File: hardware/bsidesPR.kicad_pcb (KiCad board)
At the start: 2 copper layers, 136 x 120.2 mm, 76 parts, among them J2 Conn_ARM_SWD_TagConnect_TC2030, J3 Conn_01x03_Female, Q1 2N7002H, Q2 DMP2012SN-7, SW1 SW_MEC_5G, U1 Pico, U2 TPS61040DDC

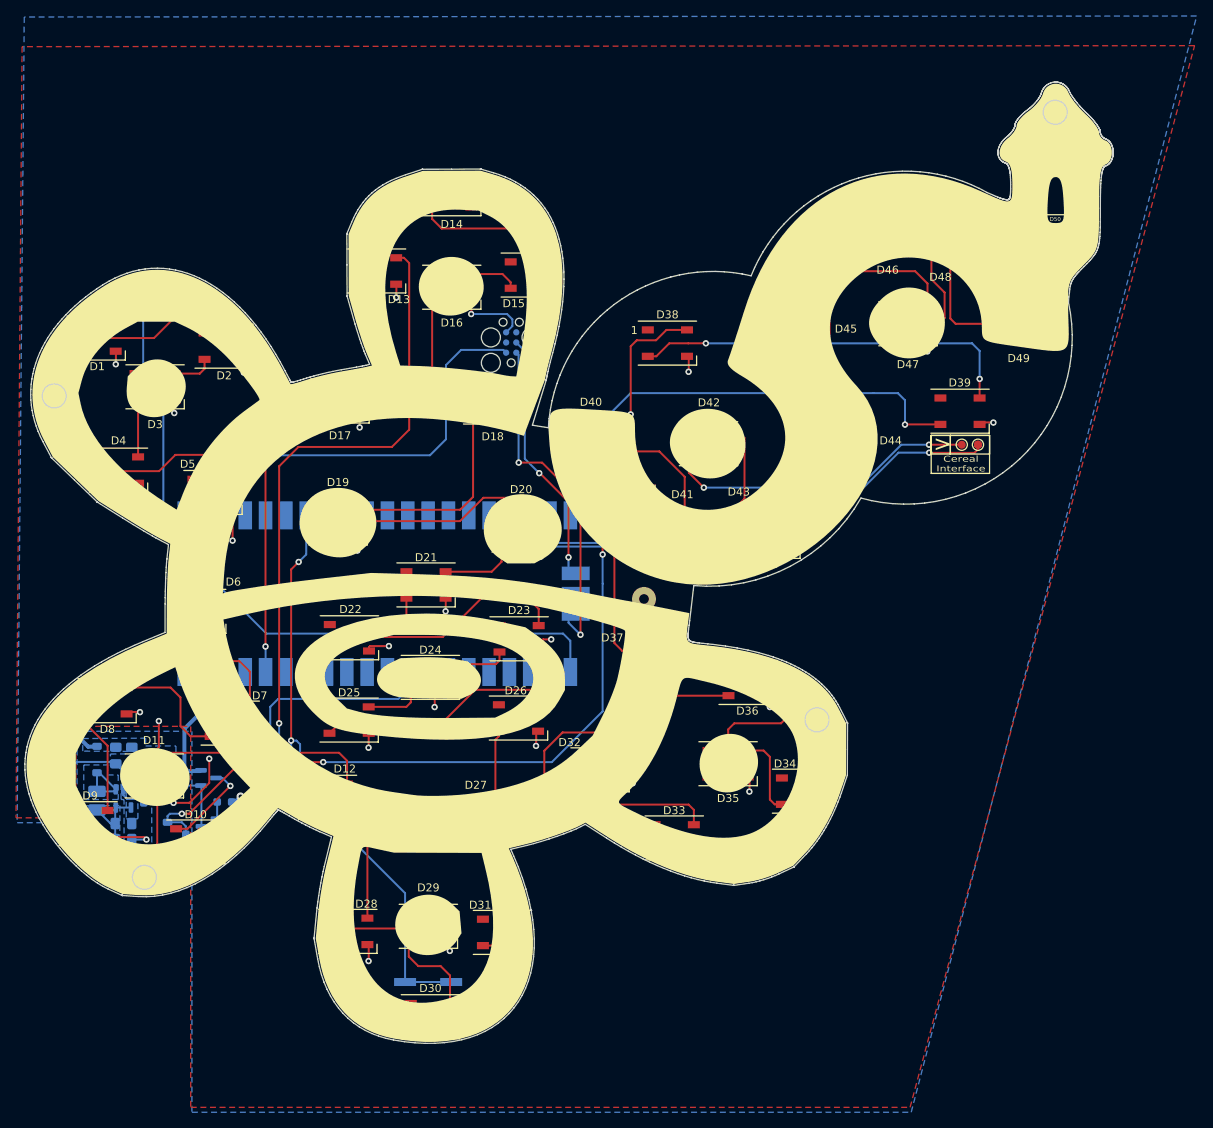
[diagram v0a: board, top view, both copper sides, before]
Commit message: Adding some animation support as well as final hardware files
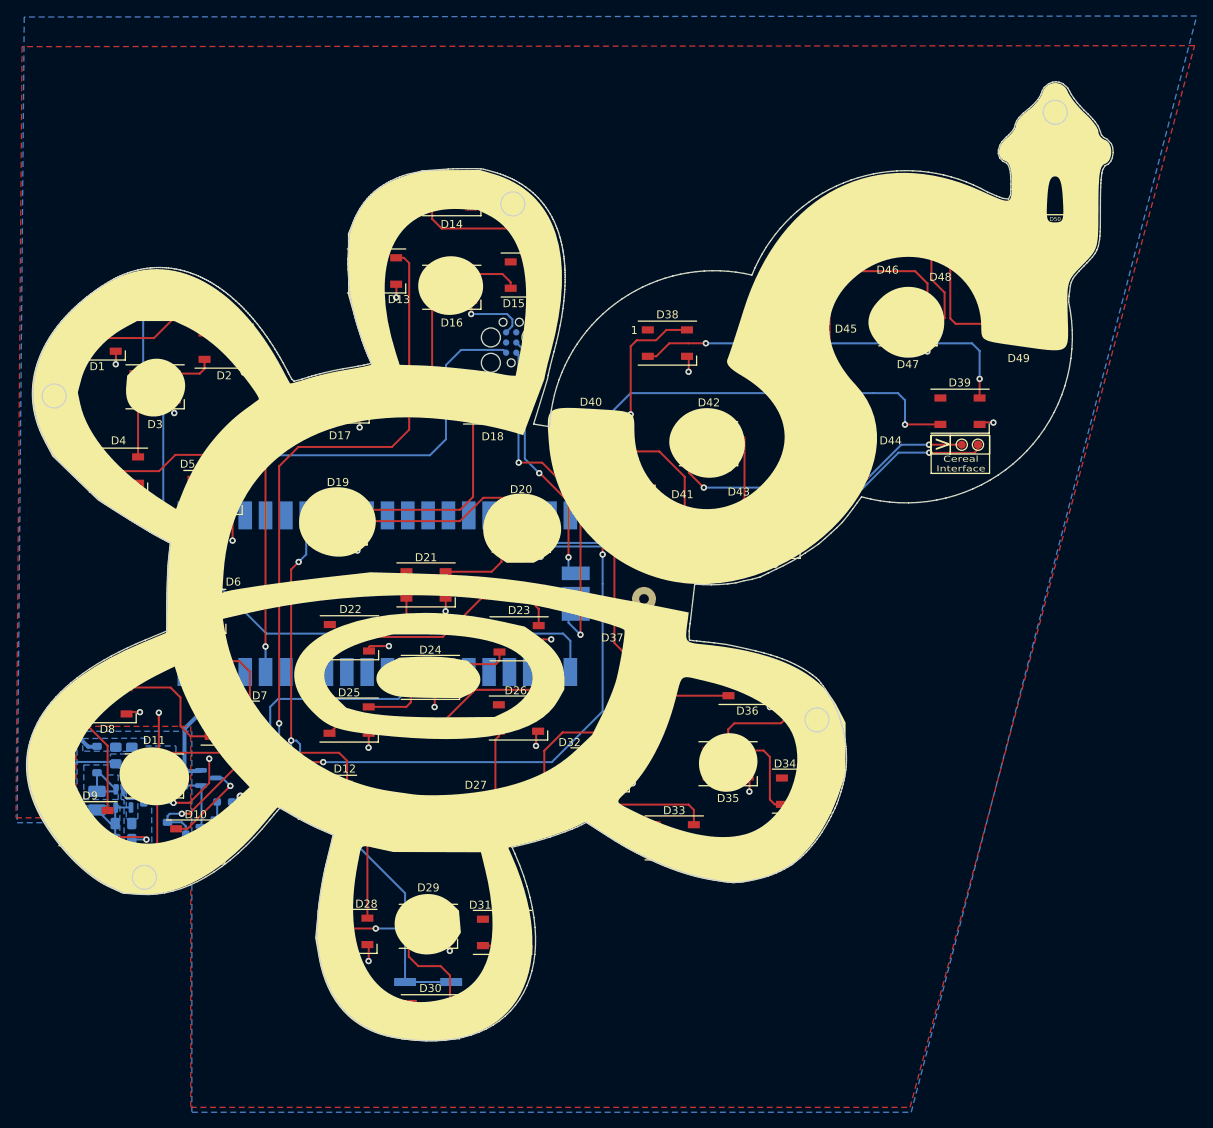
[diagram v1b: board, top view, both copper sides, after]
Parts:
- removed the G*** at (178.9, 67.5)
- added G***: LOGO, LOGO, B.Cu at (164.9, 67.6)
- added G***: LOGO, LOGO, B.Cu at (128.8, 137.9)
- added G***: LOGO, LOGO, B.Cu at (96.3, 72.4)
- added G***: LOGO, LOGO, B.Cu at (194.8, 60.5)
- added G***: LOGO, LOGO, B.Cu at (165.6, 118.6)
- added G***: LOGO, LOGO, B.Cu at (140.7, 57.2)
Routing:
- net VLED: track 18.5 -> 20.4 mm
- net Net-(D28-DOUT): track 16.6 -> 17.2 mm, vias 0 -> 2
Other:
- board size 136 x 120.2 mm -> 135.8 x 119.9 mm
- board text added: "Badge brought to you by: @So11Deo6loria @nathantsmith @Kshockles @yoyo_bond @headinthebooth"
- board text added: "https://github.com/So11Deo6loria/bsidesPRSun"
- board text removed: "<YOUR LOGO HERE>"
- board text removed: "Badge brought to you by: @So11Deo6loria @Nate_Sm1th @kshock @YoYo @headinthebooth"

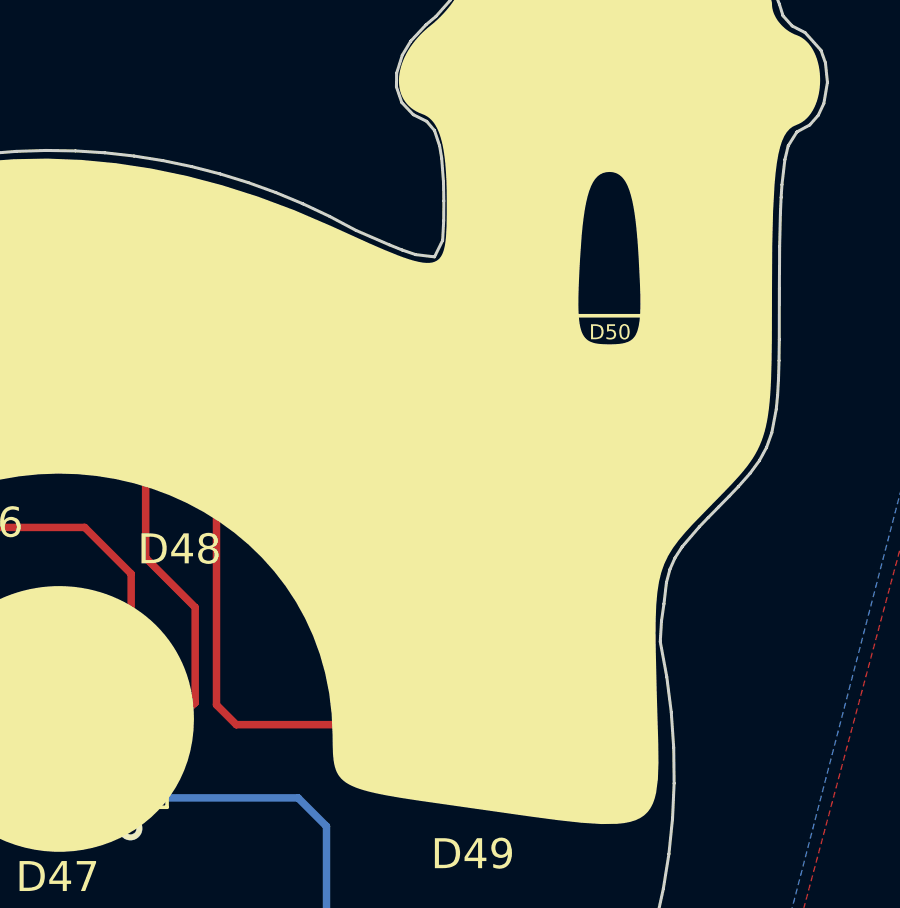
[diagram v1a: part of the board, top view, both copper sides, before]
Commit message: Firmware is close. We just need to add the flags, test one more time, and add back the lowpower stuff that messes with rshell.
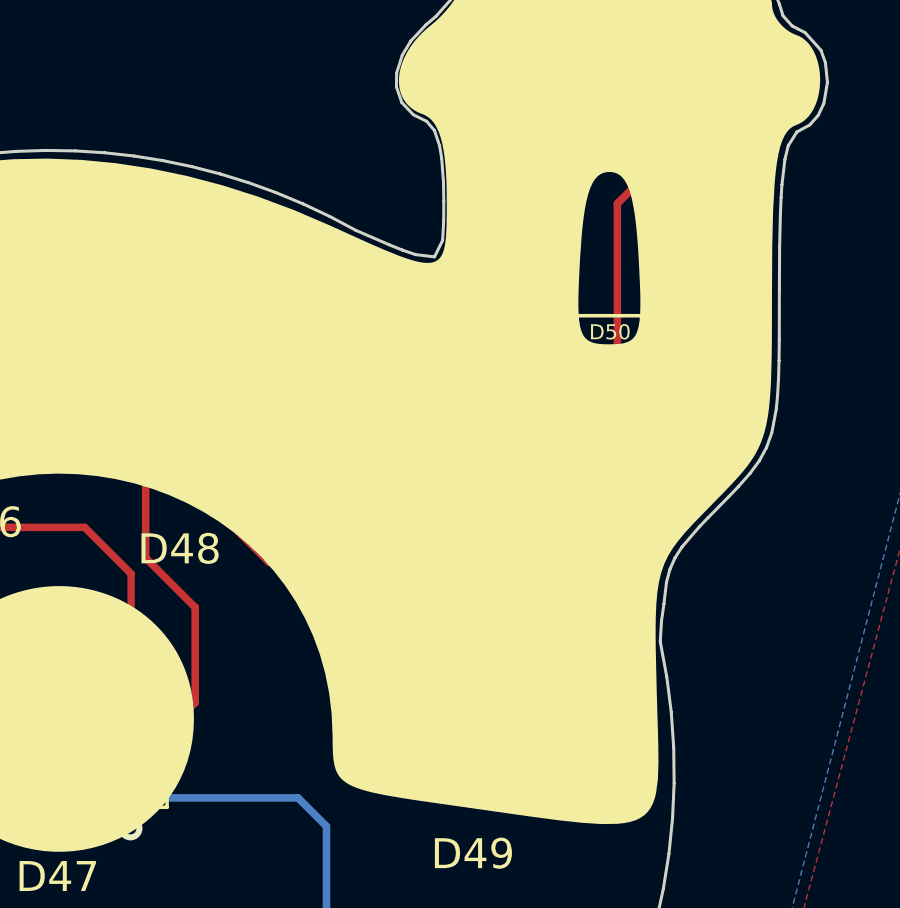
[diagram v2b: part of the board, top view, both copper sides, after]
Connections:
- D49 pad 2: Net-(D48-DOUT) -> Net-(D49-DOUT)
- D49 pad 4: Net-(D49-DIN) -> Net-(D48-DOUT)
- D50 pad 2: Net-(D49-DIN) -> unconnected-(D50-DOUT-Pad2)
- D50 pad 4: unconnected-(D50-DIN-Pad4) -> Net-(D49-DOUT)
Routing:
- net Net-(D49-DOUT): track 0.00 -> 25.6 mm
- net Net-(D49-DIN): track 11.6 -> 0.00 mm
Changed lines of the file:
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@@
   (net 77 "Net-(D25-DOUT)")
   (net 78 "Net-(D26-DOUT)")
-  (net 79 "unconnected-(D50-DIN-Pad4)")
-  (net 80 "Net-(D49-DIN)")
+  (net 79 "Net-(D49-DOUT)")
+  (net 80 "unconnected-(D50-DOUT-Pad2)")
   (net 81 "Net-(D43-DOUT)")
   (net 82 "Net-(D32-DOUT)")
@@
       (net 20 "VLED") (pinfunction "VDD") (pintype "power_in"))
     (pad "2" smd rect (at -2.45 1.65) (size 1.5 0.9) (layers "F.Cu" "F.Paste" "F.Mask")
-      (net 80 "Net-(D49-DIN)") (pinfunction "DOUT") (pintype "output"))
+      (net 80 "unconnected-(D50-DOUT-Pad2)") (pinfunction "DOUT") (pintype "output"))
     (pad "3" smd rect (at 2.45 1.65) (size 1.5 0.9) (layers "F.Cu" "F.Paste" "F.Mask")
       (net 1 "GND") (pinfunction "VSS") (pintype "power_in"))
     (pad "4" smd rect (at 2.45 -1.65) (size 1.5 0.9) (layers "F.Cu" "F.Paste" "F.Mask")
-      (net 79 "unconnected-(D50-DIN-Pad4)") (pinfunction "DIN") (pintype "input"))
+      (net 79 "Net-(D49-DOUT)") (pinfunction "DIN") (pintype "input"))
     (model "${KICAD7_3DMODEL_DIR}/LED_SMD.3dshapes/LED_WS2812B_PLCC4_5.0x5.0mm_P3.2mm.wrl"
       (offset (xyz 0 0 0))
@@
       (net 20 "VLED") (pinfunction "VDD") (pintype "power_in"))
     (pad "2" smd rect (at -2.45 1.65) (size 1.5 0.9) (layers "F.Cu" "F.Paste" "F.Mask")
-      (net 42 "Net-(D48-DOUT)") (pinfunction "DOUT") (pintype "output"))
+      (net 79 "Net-(D49-DOUT)") (pinfunction "DOUT") (pintype "output"))
     (pad "3" smd rect (at 2.45 1.65) (size 1.5 0.9) (layers "F.Cu" "F.Paste" "F.Mask")
       (net 1 "GND") (pinfunction "VSS") (pintype "power_in"))
     (pad "4" smd rect (at 2.45 -1.65) (size 1.5 0.9) (layers "F.Cu" "F.Paste" "F.Mask")
-      (net 80 "Net-(D49-DIN)") (pinfunction "DIN") (pintype "input"))
+      (net 42 "Net-(D48-DOUT)") (pinfunction "DIN") (pintype "input"))
     (model "${KICAD7_3DMODEL_DIR}/LED_SMD.3dshapes/LED_WS2812B_PLCC4_5.0x5.0mm_P3.2mm.wrl"
       (offset (xyz 0 0 0))
@@
   (segment (start 192.040172 54.000901) (end 193.945172 52.095901) (width 0.25) (layer "F.Cu") (net 41))
   (segment (start 192.929172 64.795901) (end 193.691172 64.033901) (width 0.25) (layer "F.Cu") (net 41))
-  (segment (start 194.4 64.107729) (end 194.4 53.974) (width 0.25) (layer "F.Cu") (net 42))
-  (segment (start 195.060271 64.768) (end 194.4 64.107729) (width 0.25) (layer "F.Cu") (net 42))
-  (segment (start 200.66 64.768) (end 195.060271 64.768) (width 0.25) (layer "F.Cu") (net 42))
+  (segment (start 194.4 57.605329) (end 196.154972 59.360301) (width 0.25) (layer "F.Cu") (net 42))
+  (segment (start 204.613172 59.360301) (end 205.56 60.307129) (width 0.25) (layer "F.Cu") (net 42))
+  (segment (start 205.56 60.307129) (end 205.56 61.468) (width 0.25) (layer "F.Cu") (net 42))
+  (segment (start 194.4 53.974) (end 194.4 57.605329) (width 0.25) (layer "F.Cu") (net 42))
+  (segment (start 196.154972 59.360301) (end 204.613172 59.360301) (width 0.25) (layer "F.Cu") (net 42))
   (segment (start 150.942972 93.599501) (end 150.942972 87.528901) (width 0.25) (layer "F.Cu") (net 43))
   (segment (start 99.253972 126.009901) (end 105.705572 119.558301) (width 0.25) (layer "F.Cu") (net 43))
@@
   (segment (start 137.975 115.695) (end 137.975 116.321073) (width 0.25) (layer "F.Cu") (net 78))
   (segment (start 137.541 116.755073) (end 137.541 125.222) (width 0.25) (layer "F.Cu") (net 78))
-  (segment (start 205.56 61.468) (end 205.56 55.963729) (width 0.25) (layer "F.Cu") (net 80))
-  (segment (start 205.56 55.963729) (end 205.068 55.471729) (width 0.25) (layer "F.Cu") (net 80))
-  (segment (start 205.068 55.471729) (end 205.068 50.037) (width 0.25) (layer "F.Cu") (net 80))
+  (segment (start 202.054499 63.373501) (end 206.848372 63.373501) (width 0.25) (layer "F.Cu") (net 79))
+  (segment (start 207.762772 62.459101) (end 207.762772 47.396901) (width 0.25) (layer "F.Cu") (net 79))
+  (segment (start 206.848372 63.373501) (end 207.762772 62.459101) (width 0.25) (layer "F.Cu") (net 79))
+  (segment (start 207.762772 47.396901) (end 208.422673 46.737) (width 0.25) (layer "F.Cu") (net 79))
+  (segment (start 208.422673 46.737) (end 209.968 46.737) (width 0.25) (layer "F.Cu") (net 79))
+  (segment (start 200.66 64.768) (end 202.054499 63.373501) (width 0.25) (layer "F.Cu") (net 79))
   (segment (start 184.166172 78.384901) (end 183.379271 77.598) (width 0.25) (layer "F.Cu") (net 81))
   (segment (start 184.166172 83.845901) (end 184.166172 78.384901) (width 0.25) (layer "F.Cu") (net 81))
